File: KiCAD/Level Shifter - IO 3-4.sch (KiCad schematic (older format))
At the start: 143 parts, among them Q17 MMBT3904, Q18 MMBT3906, Q19 DMG1029SV, Q20 MMBT3904, Q21 MMBT3906, Q22 DMG1029SV, Q23 MMBT3904, Q24 DMN63D8LDW, U22 MCP4728A2, U23 NCV20074, U24 TS3011, U25 MCP4725A1, U26 TS3011, U27 PI5A3157, U28 LM7171, U29 LM7171, U30 LM7171, U31 PI5A3157, U32 LM7171, U33 LM7171, U34 DG448DV, U35 DG448DV

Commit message: Add power changeover circuit, fix minor issues
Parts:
- C81, C82, C85, R195, R196, R209: value 0 -> C
- C88, C89, C94, C95, C96, C97: value 10u -> 0.1u
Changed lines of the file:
@@
 Sheet 8 10
 Title "LEVEL SHIFTER SUBSYSTEM - I/O PINS 3 & 4"
-Date "2020-02-03"
+Date "2020-02-04"
 Rev "A"
 Comp "THE UNIVERSITY OF AKRON"
@@
 P 10900 7850
 F 0 "C94" H 11015 7896 50  0000 L CNN
-F 1 "10u" H 11015 7805 50  0000 L CNN
+F 1 "0.1u" H 11015 7805 50  0000 L CNN
 F 2 "" H 10938 7700 50  0001 C CNN
 F 3 "~" H 10900 7850 50  0001 C CNN
@@
 P 10900 8250
 F 0 "C95" H 11015 8296 50  0000 L CNN
-F 1 "10u" H 11015 8205 50  0000 L CNN
+F 1 "0.1u" H 11015 8205 50  0000 L CNN
 F 2 "" H 10938 8100 50  0001 C CNN
 F 3 "~" H 10900 8250 50  0001 C CNN
@@
 P 8350 6400
 F 0 "C88" H 8465 6446 50  0000 L CNN
-F 1 "10u" H 8465 6355 50  0000 L CNN
+F 1 "0.1u" H 8465 6355 50  0000 L CNN
 F 2 "" H 8388 6250 50  0001 C CNN
 F 3 "~" H 8350 6400 50  0001 C CNN
@@
 P 8350 6800
 F 0 "C89" H 8465 6846 50  0000 L CNN
-F 1 "10u" H 8465 6755 50  0000 L CNN
+F 1 "0.1u" H 8465 6755 50  0000 L CNN
 F 2 "" H 8388 6650 50  0001 C CNN
 F 3 "~" H 8350 6800 50  0001 C CNN
@@
 P 10950 1500
 F 0 "C96" H 11065 1546 50  0000 L CNN
-F 1 "10u" H 11065 1455 50  0000 L CNN
+F 1 "0.1u" H 11065 1455 50  0000 L CNN
 F 2 "" H 10988 1350 50  0001 C CNN
 F 3 "~" H 10950 1500 50  0001 C CNN
@@
 P 10950 1900
 F 0 "C97" H 11065 1946 50  0000 L CNN
-F 1 "10u" H 11065 1855 50  0000 L CNN
+F 1 "0.1u" H 11065 1855 50  0000 L CNN
 F 2 "" H 10988 1750 50  0001 C CNN
 F 3 "~" H 10950 1900 50  0001 C CNN
@@
 P 6050 3500
 F 0 "R195" V 5950 3500 50  0000 C CNN
-F 1 "0" V 6050 3500 50  0001 C CNN
+F 1 "C" V 6050 3500 50  0001 C CNN
 F 2 "" V 5980 3500 50  0001 C CNN
 F 3 "~" H 6050 3500 50  0001 C CNN
@@
 P 6450 3500
 F 0 "C81" V 6300 3500 50  0000 C CNN
-F 1 "0" V 6300 3600 50  0001 C CNN
+F 1 "C" V 6300 3600 50  0001 C CNN
 F 2 "" H 6488 3350 50  0001 C CNN
 F 3 "~" H 6450 3500 50  0001 C CNN
@@
 P 6250 6750
 F 0 "R196" V 6150 6750 50  0000 C CNN
-F 1 "0" V 6250 6750 50  0001 C CNN
+F 1 "C" V 6250 6750 50  0001 C CNN
 F 2 "" V 6180 6750 50  0001 C CNN
 F 3 "~" H 6250 6750 50  0001 C CNN
@@
 P 6650 6750
 F 0 "C82" V 6500 6750 50  0000 C CNN
-F 1 "0" V 6500 6850 50  0001 C CNN
+F 1 "C" V 6500 6850 50  0001 C CNN
 F 2 "" H 6688 6600 50  0001 C CNN
 F 3 "~" H 6650 6750 50  0001 C CNN
@@
 P 7850 7900
 F 0 "R209" V 7750 7900 50  0000 C CNN
-F 1 "0" V 7850 7900 50  0001 C CNN
+F 1 "C" V 7850 7900 50  0001 C CNN
 F 2 "" V 7780 7900 50  0001 C CNN
 F 3 "~" H 7850 7900 50  0001 C CNN
@@
 P 8250 7900
 F 0 "C85" V 8100 7900 50  0000 C CNN
-F 1 "0" V 8100 8000 50  0001 C CNN
+F 1 "C" V 8100 8000 50  0001 C CNN
 F 2 "" H 8288 7750 50  0001 C CNN
 F 3 "~" H 8250 7900 50  0001 C CNN

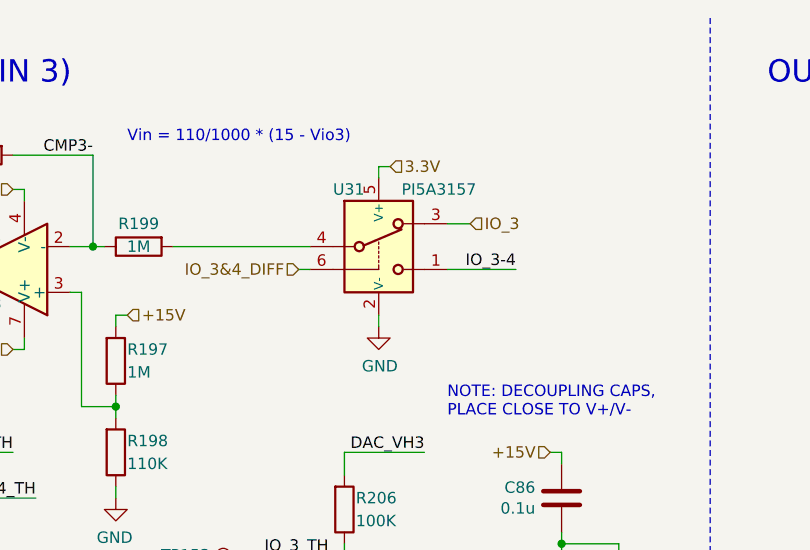
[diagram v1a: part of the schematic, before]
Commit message: Replace switches U14 and U31 with higher voltage part
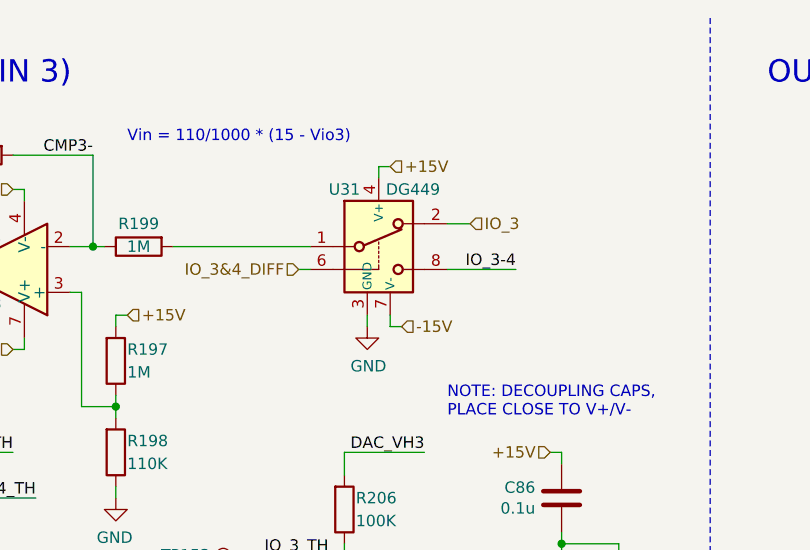
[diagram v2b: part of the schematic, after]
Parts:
- removed U31: PI5A3157, Package_TO_SOT_SMD:SOT-363_SC-70-6, symbol io-master:PI5A3157
- added U31: DG449, Package_TO_SOT_SMD:SOT-23-8, symbol io-master:DG449
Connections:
- net +15V: now also U31.4 (V+)
- net -15V: now also U31.7 (V-)
- net CMP+: now also U31.8
- net GND: now also U31.3 (GND)
- net IO_3: now also U31.2
- net IO_3&4_DIFF: now also U31.6
- net at R199.2: now also U31.1
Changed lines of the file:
@@
 Wire Wire Line
 	5300 2800 5300 2850
-$Comp
-L io-master:PI5A3157 U31
-U 1 1 5EC7D4FA
-P 7550 1400
-F 0 "U31" H 7350 1550 50  0000 L CNN
-F 1 "PI5A3157" H 7650 1550 50  0000 L CNN
-F 2 "Package_TO_SOT_SMD:SOT-363_SC-70-6" H 7550 1100 50  0001 C CNN
-F 3 "https://www.diodes.com/assets/Datasheets/PI5A3157.pdf" H 7550 1200 50  0001 C CNN
-	1    7550 1400
-	1    0    0    -1
-$EndComp
 Wire Wire Line
 	7200 1600 7250 1600
@@
 L power:GND #PWR0118
 U 1 1 5EC7D506
-P 7550 1850
-F 0 "#PWR0118" H 7550 1600 50  0001 C CNN
-F 1 "GND" H 7555 1677 50  0000 C CNN
-F 2 "" H 7550 1850 50  0001 C CNN
-F 3 "" H 7550 1850 50  0001 C CNN
-	1    7550 1850
-	1    0    0    -1
-$EndComp
-Text HLabel 7600 1150 2    50   Input ~ 0
-3.3V
+P 7500 1850
+F 0 "#PWR0118" H 7500 1600 50  0001 C CNN
+F 1 "GND" H 7505 1677 50  0000 C CNN
+F 2 "" H 7500 1850 50  0001 C CNN
+F 3 "" H 7500 1850 50  0001 C CNN
+	1    7500 1850
+	1    0    0    -1
+$EndComp
 Wire Wire Line
 	7600 1150 7550 1150
@@
 	7550 1150 7550 1200
 Wire Wire Line
-	7550 1800 7550 1850
+	7500 1800 7500 1850
 Text HLabel 7200 1600 0    50   Input ~ 0
 IO_3&4_DIFF
@@
 Wire Wire Line
 	15050 4850 15100 4850
+$Comp
+L io-master:DG449 U31
+U 1 1 5E4A8A52
+P 7550 1400
+F 0 "U31" H 7400 1550 50  0000 C CNN
+F 1 "DG449" H 7700 1550 50  0000 C CNN
+F 2 "Package_TO_SOT_SMD:SOT-23-8" H 7550 1100 50  0001 C CNN
+F 3 "http://www.vishay.com/docs/73897/dg449.pdf" H 7550 1200 50  0001 C CNN
+	1    7550 1400
+	1    0    0    -1
+$EndComp
+Text HLabel 7600 1150 2    50   Input ~ 0
++15V
+Text HLabel 7650 1850 2    50   Input ~ 0
+-15V
+Wire Wire Line
+	7650 1850 7600 1850
+Wire Wire Line
+	7600 1850 7600 1800
 $EndSCHEMATC

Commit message: Assign footprints, fix minor schematic issues
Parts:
- C73, C74, C75, C76, C77, C78, C79, C80, C81, C82, C83, C84, C85, C86, C87, C88, C89, C94, C95, C96, C97, C98: footprint (none) -> Capacitor_SMD:C_0603_1608Metric
- C90, C91, C92, C93: footprint (none) -> Capacitor_SMD:C_0805_2012Metric
- D28, D29: footprint (none) -> Diode_SMD:D_SOD-323
- Q17, Q18, Q20, Q21, Q23: footprint Package_TO_SOT_SMD:SOT-23 -> Package_TO_SOT_SMD:SOT-323_SC-70
- R168, R169, R170, R171, R172, R173, R174, R175, R176, R177, R178, R179, R180, R181, R182, R183, R184, R185, R186, R187, R188, R189, R190, R191, R192, R193, R194, R197, R198, R199, R200, R201, R202, R203, R204, R205, R206, R207, R208, R210, R211, R212, R213, R214, R215, R216, R217, R218, R219, R220, R221, R222, R223, R224, R225, R226, R227, R228, R229, R230, R231, R232, R233, R234, R235, R236: footprint (none) -> Resistor_SMD:R_0603_1608Metric
- R195, R196, R209: value C -> R; footprint (none) -> Resistor_SMD:R_0603_1608Metric
- R237, R238, R239, R240: footprint (none) -> Resistor_SMD:R_0805_2012Metric
- TP141: value TestPoint -> DVH3; footprint (none) -> TestPoint:TestPoint_Pad_D1.0mm
- TP142: value TestPoint -> DVL3; footprint (none) -> TestPoint:TestPoint_Pad_D1.0mm
- TP143: value TestPoint -> DVH4; footprint (none) -> TestPoint:TestPoint_Pad_D1.0mm
- TP144: value TestPoint -> DVL4; footprint (none) -> TestPoint:TestPoint_Pad_D1.0mm
- TP145: value TestPoint -> VH3; footprint (none) -> TestPoint:TestPoint_Pad_D1.0mm
- TP146: value TestPoint -> VL3; footprint (none) -> TestPoint:TestPoint_Pad_D1.0mm
- TP147: value TestPoint -> VH4; footprint (none) -> TestPoint:TestPoint_Pad_D1.0mm
- TP148: value TestPoint -> VL4; footprint (none) -> TestPoint:TestPoint_Pad_D1.0mm
- TP149, TP150, TP154, TP155, TP156, TP157, TP158, TP159, TP160: footprint (none) -> TestPoint:TestPoint_Pad_D1.0mm
- TP151: value TestPoint -> TH34; footprint (none) -> TestPoint:TestPoint_Pad_D1.0mm
- TP152: value TestPoint -> 3-4; footprint (none) -> TestPoint:TestPoint_Pad_D1.0mm
- TP153: value TestPoint -> TH3; footprint (none) -> TestPoint:TestPoint_Pad_D1.0mm

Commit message: Add C18 and C21 0.1u decoupling caps, fix minor issues
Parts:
- added C21: 0.1u, Capacitor_SMD:C_0603_1608Metric, symbol Device:C
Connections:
- net +15V: now also C80.1
- net -15V: now also C21.2
- net 3.3V: no longer C80.1
- net GND: now also C21.1
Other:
- moved on the sheet: C76, C78, C86, C87
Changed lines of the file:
@@
 Sheet 8 10
 Title "LEVEL SHIFTER SUBSYSTEM - I/O PINS 3 & 4"
-Date "2020-02-07"
+Date "2020-02-10"
 Rev "A"
 Comp "THE UNIVERSITY OF AKRON"
@@
 L Device:C C76
 U 1 1 5FC14AD3
-P 4000 3100
-F 0 "C76" H 4115 3146 50  0000 L CNN
-F 1 "0.1u" H 4115 3055 50  0000 L CNN
-F 2 "Capacitor_SMD:C_0603_1608Metric" H 4038 2950 50  0001 C CNN
-F 3 "~" H 4000 3100 50  0001 C CNN
-	1    4000 3100
+P 4100 3100
+F 0 "C76" H 4215 3146 50  0000 L CNN
+F 1 "0.1u" H 4215 3055 50  0000 L CNN
+F 2 "Capacitor_SMD:C_0603_1608Metric" H 4138 2950 50  0001 C CNN
+F 3 "~" H 4100 3100 50  0001 C CNN
+	1    4100 3100
 	1    0    0    -1
 $EndComp
@@
 L power:GND #PWR0108
 U 1 1 5FC14AD4
-P 4000 3350
-F 0 "#PWR0108" H 4000 3100 50  0001 C CNN
-F 1 "GND" H 4005 3177 50  0000 C CNN
-F 2 "" H 4000 3350 50  0001 C CNN
-F 3 "" H 4000 3350 50  0001 C CNN
-	1    4000 3350
+P 4100 3350
+F 0 "#PWR0108" H 4100 3100 50  0001 C CNN
+F 1 "GND" H 4105 3177 50  0000 C CNN
+F 2 "" H 4100 3350 50  0001 C CNN
+F 3 "" H 4100 3350 50  0001 C CNN
+	1    4100 3350
 	1    0    0    -1
 $EndComp
 Wire Wire Line
-	4000 3350 4000 3300
+	4100 3350 4100 3300
 Wire Wire Line
-	4000 2900 4000 2950
+	4100 2900 4100 2950
 Text Notes 3850 3800 0    50   ~ 0
 NOTE: DECOUPLING CAPS,\nPLACE CLOSE TO V+
-Text HLabel 3950 2900 0    50   Input ~ 0
+Text HLabel 4050 2900 0    50   Input ~ 0
 3.3V
 Wire Wire Line
-	3950 2900 4000 2900
+	4050 2900 4100 2900
 $Comp
 L Device:C C86
 U 1 1 5FC14AD5
-P 8350 2600
-F 0 "C86" H 8465 2646 50  0000 L CNN
-F 1 "0.1u" H 8465 2555 50  0000 L CNN
-F 2 "Capacitor_SMD:C_0603_1608Metric" H 8388 2450 50  0001 C CNN
-F 3 "~" H 8350 2600 50  0001 C CNN
-	1    8350 2600
+P 8250 2600
+F 0 "C86" H 8365 2646 50  0000 L CNN
+F 1 "0.1u" H 8365 2555 50  0000 L CNN
+F 2 "Capacitor_SMD:C_0603_1608Metric" H 8288 2450 50  0001 C CNN
+F 3 "~" H 8250 2600 50  0001 C CNN
+	1    8250 2600
 	-1   0    0    -1
 $EndComp
@@
 L power:GND #PWR0122
 U 1 1 5FC14AD6
-P 8600 2850
-F 0 "#PWR0122" H 8600 2600 50  0001 C CNN
-F 1 "GND" H 8605 2677 50  0000 C CNN
-F 2 "" H 8600 2850 50  0001 C CNN
-F 3 "" H 8600 2850 50  0001 C CNN
-	1    8600 2850
+P 8800 2850
+F 0 "#PWR0122" H 8800 2600 50  0001 C CNN
+F 1 "GND" H 8805 2677 50  0000 C CNN
+F 2 "" H 8800 2850 50  0001 C CNN
+F 3 "" H 8800 2850 50  0001 C CNN
+	1    8800 2850
 	1    0    0    -1
 $EndComp
 Wire Wire Line
-	8350 2400 8350 2450
+	8250 2400 8250 2450
 Text Notes 7850 2250 0    50   ~ 0
 NOTE: DECOUPLING CAPS,\nPLACE CLOSE TO V+/V-
 Wire Wire Line
-	8300 2400 8350 2400
+	8200 2400 8250 2400
 $Comp
 L Device:C C87
 U 1 1 5FC14AD7
-P 8350 3000
-F 0 "C87" H 8465 3046 50  0000 L CNN
-F 1 "0.1u" H 8465 2955 50  0000 L CNN
-F 2 "Capacitor_SMD:C_0603_1608Metric" H 8388 2850 50  0001 C CNN
-F 3 "~" H 8350 3000 50  0001 C CNN
-	1    8350 3000
+P 8250 3000
+F 0 "C87" H 8365 3046 50  0000 L CNN
+F 1 "0.1u" H 8365 2955 50  0000 L CNN
+F 2 "Capacitor_SMD:C_0603_1608Metric" H 8288 2850 50  0001 C CNN
+F 3 "~" H 8250 3000 50  0001 C CNN
+	1    8250 3000
 	-1   0    0    -1
 $EndComp
 Wire Wire Line
-	8350 2750 8350 2800
+	8250 2750 8250 2800
 Wire Wire Line
-	8300 3200 8350 3200
+	8200 3200 8250 3200
 Wire Wire Line
-	8350 3200 8350 3150
-Connection ~ 8350 2800
+	8250 3200 8250 3150
+Connection ~ 8250 2800
 Wire Wire Line
-	8350 2800 8350 2850
-Wire Wire Line
-	8600 2800 8600 2850
-Wire Wire Line
-	8350 2800 8600 2800
-Text HLabel 8300 2400 0    50   Input ~ 0
+	8250 2800 8250 2850
+Text HLabel 8200 2400 0    50   Input ~ 0
 +15V
-Text HLabel 8300 3200 0    50   Input ~ 0
+Text HLabel 8200 3200 0    50   Input ~ 0
 -15V
 $Comp
@@
 L Device:C C78
 U 1 1 6023356A
-P 4400 3100
-F 0 "C78" H 4515 3146 50  0000 L CNN
-F 1 "0.1u" H 4515 3055 50  0000 L CNN
-F 2 "Capacitor_SMD:C_0603_1608Metric" H 4438 2950 50  0001 C CNN
-F 3 "~" H 4400 3100 50  0001 C CNN
-	1    4400 3100
+P 4500 3100
+F 0 "C78" H 4615 3146 50  0000 L CNN
+F 1 "0.1u" H 4615 3055 50  0000 L CNN
+F 2 "Capacitor_SMD:C_0603_1608Metric" H 4538 2950 50  0001 C CNN
+F 3 "~" H 4500 3100 50  0001 C CNN
+	1    4500 3100
 	1    0    0    -1
 $EndComp
-$Comp
-L Device:C C80
-U 1 1 602338F0
-P 4800 3100
-F 0 "C80" H 4915 3146 50  0000 L CNN
-F 1 "0.1u" H 4915 3055 50  0000 L CNN
-F 2 "Capacitor_SMD:C_0603_1608Metric" H 4838 2950 50  0001 C CNN
-F 3 "~" H 4800 3100 50  0001 C CNN
-	1    4800 3100
-	1    0    0    -1
-$EndComp
-Wire Wire Line
-	4000 2900 4400 2900
 Wire Wire Line
-	4800 2900 4800 2950
-Connection ~ 4000 2900
+	4100 2900 4500 2900
+Connection ~ 4100 2900
 Wire Wire Line
-	4400 2950 4400 2900
-Connection ~ 4400 2900
+	4500 2950 4500 2900
 Wire Wire Line
-	4400 2900 4800 2900
+	4100 3300 4500 3300
 Wire Wire Line
-	4000 3300 4400 3300
+	4500 3300 4500 3250
+Connection ~ 4100 3300
 Wire Wire Line
-	4400 3300 4400 3250
-Connection ~ 4000 3300
-Wire Wire Line
-	4000 3300 4000 3250
-Wire Wire Line
-	4400 3300 4800 3300
-Wire Wire Line
-	4800 3300 4800 3250
-Connection ~ 4400 3300
+	4100 3300 4100 3250
 Text Notes 4700 6100 0    50   ~ 0
 THRESHOLD = 1000/110 * (1.65V - Vdac)
@@
 Wire Wire Line
 	7600 1850 7600 1800
+$Comp
+L Device:C C80
+U 1 1 5F86AF33
+P 8650 2600
+F 0 "C80" H 8765 2646 50  0000 L CNN
+F 1 "0.1u" H 8765 2555 50  0000 L CNN
+F 2 "Capacitor_SMD:C_0603_1608Metric" H 8688 2450 50  0001 C CNN
+F 3 "~" H 8650 2600 50  0001 C CNN
+	1    8650 2600
+	-1   0    0    -1
+$EndComp
+$Comp
+L Device:C C21
+U 1 1 5F8DBE86
+P 8650 3000
+F 0 "C21" H 8765 3046 50  0000 L CNN
+F 1 "0.1u" H 8765 2955 50  0000 L CNN
+F 2 "Capacitor_SMD:C_0603_1608Metric" H 8688 2850 50  0001 C CNN
+F 3 "~" H 8650 3000 50  0001 C CNN
+	1    8650 3000
+	-1   0    0    -1
+$EndComp
+Wire Wire Line
+	8800 2800 8800 2850
+Wire Wire Line
+	8250 2800 8650 2800
+Wire Wire Line
+	8650 2850 8650 2800
+Connection ~ 8650 2800
+Wire Wire Line
+	8650 2800 8800 2800
+Wire Wire Line
+	8650 2800 8650 2750
+Wire Wire Line
+	8250 2400 8650 2400
+Wire Wire Line
+	8650 2400 8650 2450
+Connection ~ 8250 2400
+Wire Wire Line
+	8250 3200 8650 3200
+Wire Wire Line
+	8650 3200 8650 3150
+Connection ~ 8250 3200
 $EndSCHEMATC
